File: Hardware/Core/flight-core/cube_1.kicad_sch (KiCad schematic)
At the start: 21 parts, among them J10 Conn_01x06, J11 Conn_01x04_Socket, J12 Conn_01x04_Socket, J13 Conn_01x06, J14 MicroFit_VT_3, J8 MicroFit_VT_3, J9 Cube Orange Plus Female Header, Q1 MMBF170, Q2 MMBF170, Q3 MMBF170

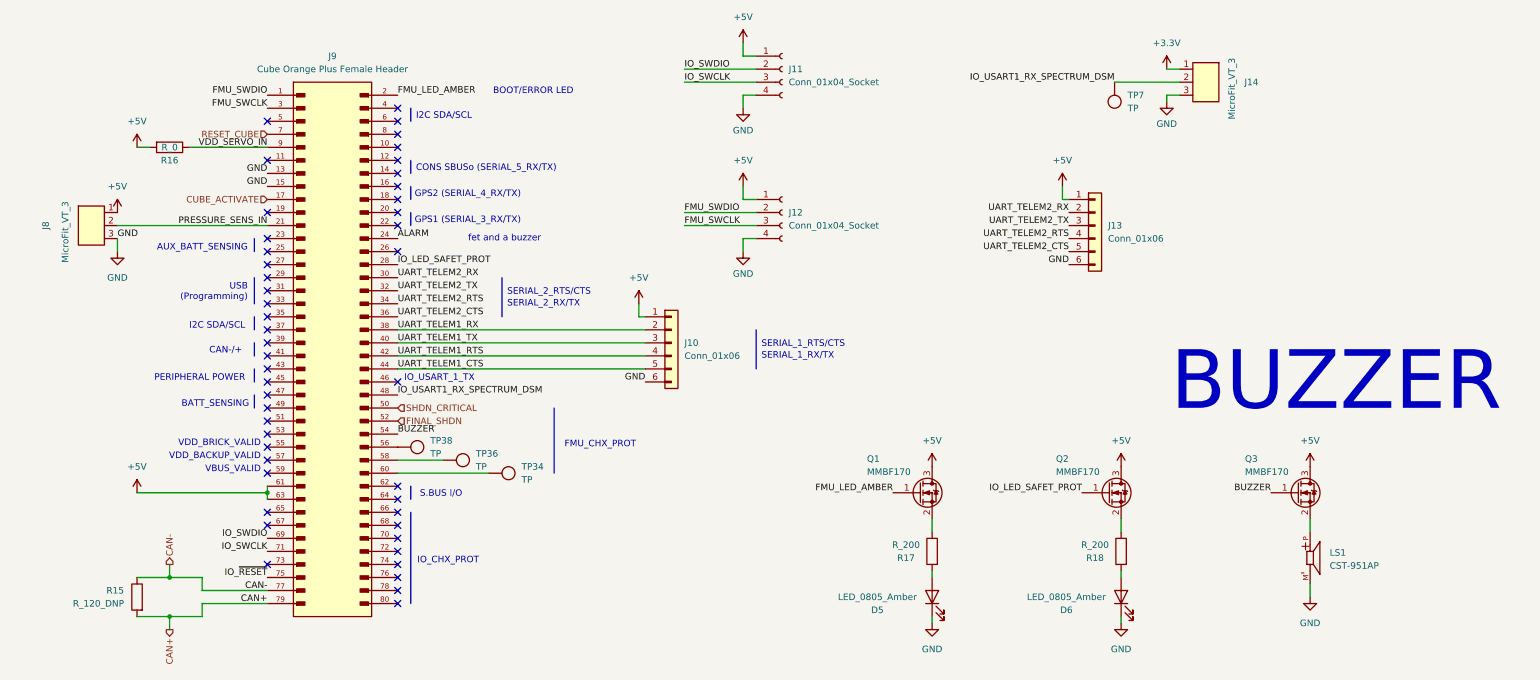
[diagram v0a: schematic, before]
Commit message: added sense pwr cycle pull down, low side cube mosfets, fixed mosi/miso swap on i/o expander, Rs -> generic, reannotated
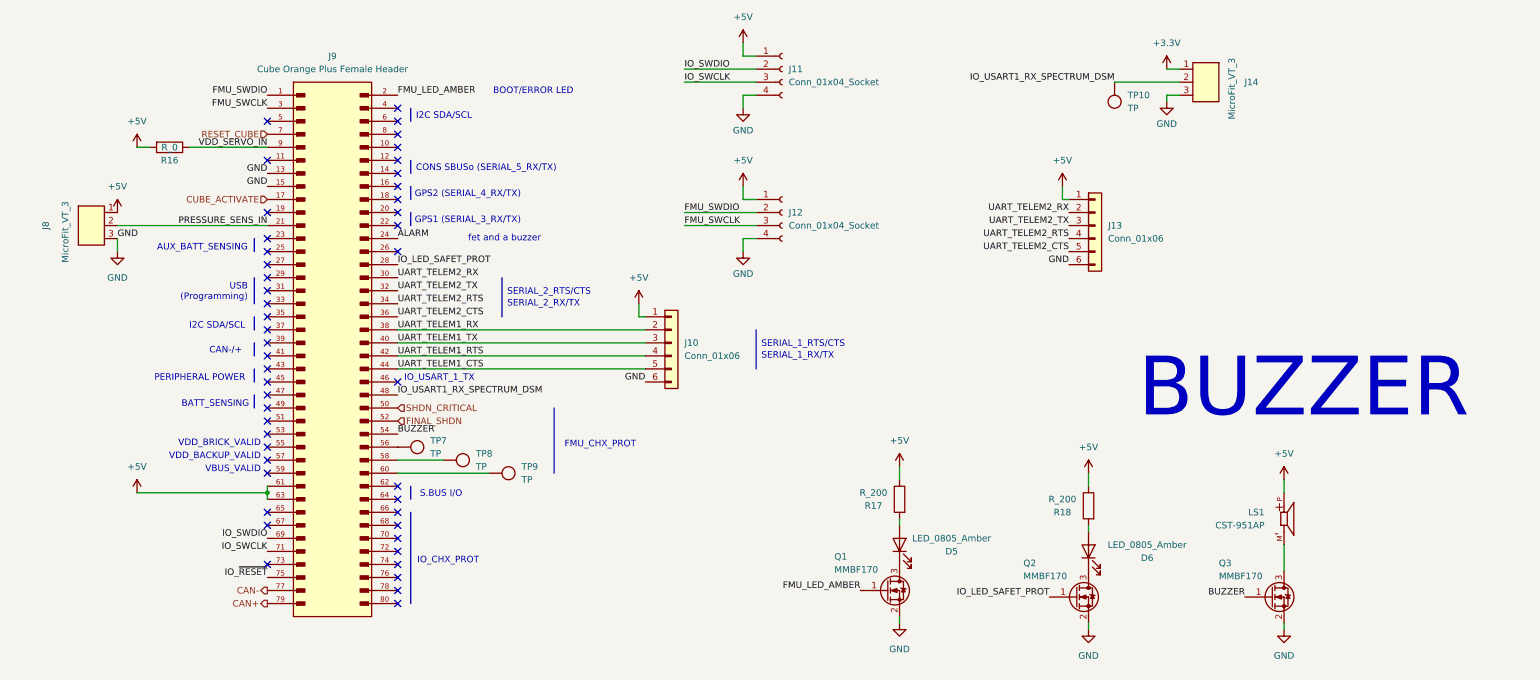
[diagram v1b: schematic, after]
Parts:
- removed R15: R_120_DNP, footprints:R_0603_1608Metric, symbol formula:R_120_DNP
- renumbered TP7 to TP10, TP38 to TP7, TP36 to TP8, TP34 to TP9
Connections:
- net +5V: now also LS1.P, R17.1, R18.1; no longer Q1.3 (D), Q2.3 (D), Q3.3 (D)
- net GND: now also Q1.2 (S), Q2.2 (S), Q3.2 (S); no longer D5.1 (K), D6.1 (K), LS1.M
- new net: LS1.M, Q3.3 (D)
- new net: D5.1 (K), Q1.3 (D)
- new net: D6.1 (K), Q2.3 (D)
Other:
- moved on the sheet: D5, D6, LS1, Q1, Q2, Q3, R17, R18

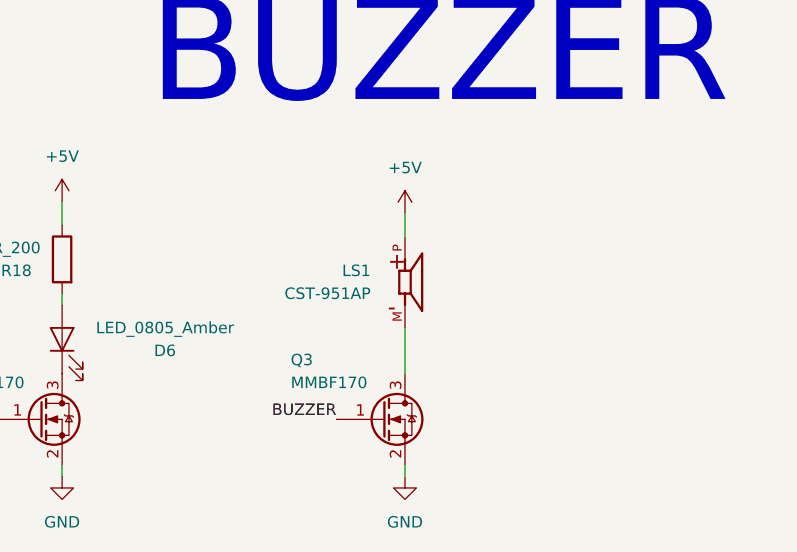
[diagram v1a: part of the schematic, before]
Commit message: replicated layout for all can repeaters, placed in shutdown order; added rider lower estop in schem; j18 is 4 pin
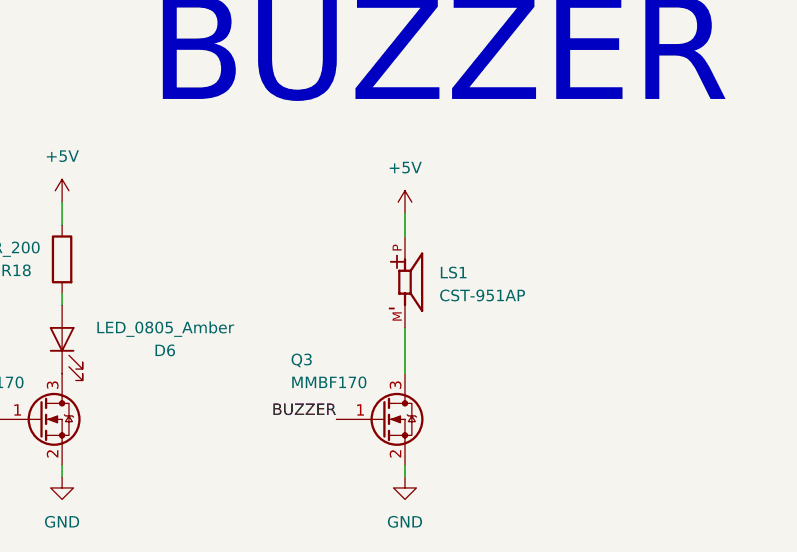
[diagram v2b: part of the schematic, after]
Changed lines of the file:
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@@
 		(dnp no)
 		(property "Reference" "LS1"
-			(at 265.43 132.08 0)
+			(at 273.05 132.327 0)
 			(effects
 				(font
 					(size 1.27 1.27)
 				)
-				(justify right)
+				(justify left)
 			)
 		)
 		(property "Value" "CST-951AP"
-			(at 265.43 134.62 0)
+			(at 273.05 134.867 0)
 			(effects
 				(font
 					(size 1.27 1.27)
 				)
-				(justify right)
+				(justify left)
 			)
 		)

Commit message: major component area placement begun, installing place footprints plugin, updating connectors to vertical
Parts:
- removed J10, J13: Conn_01x06, footprints:MicroFit_VT_6, symbol Connector_Generic:Conn_01x06
- added J10: Conn_02x06_Counter_Clockwise, Connector_Molex:Molex_Micro-Fit_3.0_43045-1212_2x06_P3.00mm_Vertical, symbol Connector_Generic:Conn_02x06_Counter_Clockwise
- renumbered J14 to J13
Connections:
- net +5V: now also J10.1 (Pin_1), J10.12 (Pin_12)
- net ALARM: now also Q3.1 (G)
- net GND: now also J10.6 (Pin_6), J10.7 (Pin_7)
- net UART_TELEM1_CTS: now also J10.5 (Pin_5)
- net UART_TELEM1_RTS: now also J10.4 (Pin_4)
- net UART_TELEM1_RX: now also J10.2 (Pin_2)
- net UART_TELEM1_TX: now also J10.3 (Pin_3)
- net UART_TELEM2_CTS: now also J10.8 (Pin_8)
- net UART_TELEM2_RTS: now also J10.9 (Pin_9)
- net UART_TELEM2_RX: now also J10.11 (Pin_11)
- net UART_TELEM2_TX: now also J10.10 (Pin_10)
- net BUZZER renamed CUBE_HANDOFF
- net CUBE_HANDOFF: no longer Q3.1 (G)
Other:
- note removed: "BUZZER"
- moved on the sheet: D5, D6, J11, J12, LS1, Q1, Q2, Q3, R17, R18

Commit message: switching test points to correct footprint and alternative symbol, moving leds
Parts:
- TP10, TP7, TP8, TP9: footprint footprints:tp_1.6mm -> TestPoint:TestPoint_Pad_D1.0mm; symbol formula:TP -> OlinBAD:D1.0_TP
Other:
- moved on the sheet: TP10, TP7, TP8, TP9
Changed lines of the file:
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@@
 	(wire
 		(pts
-			(xy 96.52 121.92) (xy 105.41 121.92)
+			(xy 96.52 121.92) (xy 111.76 121.92)
 		)
 		(stroke
@@
 	(wire
 		(pts
-			(xy 96.52 124.46) (xy 114.3 124.46)
+			(xy 96.52 124.46) (xy 116.84 124.46)
+		)
+		(stroke
+			(width 0)
+			(type default)
+		)
+	)
+	(wire
+		(pts
+			(xy 96.52 119.38) (xy 105.41 119.38)
 		)
 		(stroke
@@
 	)
 	(symbol
-		(lib_id "formula:TP")
-		(at 110.49 121.92 270)
+		(lib_id "OlinBAD:D1.0_TP")
+		(at 111.76 121.92 270)
 		(unit 1)
 		(exclude_from_sim no)
@@
 		(fields_autoplaced yes)
 		(property "Reference" "TP8"
-			(at 111.76 120.6499 90)
+			(at 116.84 120.6499 90)
 			(effects
 				(font
@@
 		)
 		(property "Value" "TP"
-			(at 111.76 123.1899 90)
+			(at 116.84 123.1899 90)
 			(effects
 				(font
@@
 			)
 		)
-		(property "Footprint" "footprints:tp_1.6mm"
-			(at 107.95 119.38 0)
-			(effects
-				(font
-					(size 1.27 1.27)
-				)
-				(hide yes)
-			)
-		)
-		(property "Datasheet" "http://www.keyelco.com/product-pdf.cfm?p=1314"
-			(at 110.49 121.92 0)
-			(effects
-				(font
-					(size 1.27 1.27)
-				)
-				(hide yes)
-			)
-		)
-		(property "Description" ""
-			(at 110.49 121.92 0)
+		(property "Footprint" "TestPoint:TestPoint_Pad_D1.0mm"
+			(at 111.76 127 0)
+			(effects
+				(font
+					(size 1.27 1.27)
+				)
+				(hide yes)
+			)
+		)
+		(property "Datasheet" "~"
+			(at 111.76 127 0)
+			(effects
+				(font
+					(size 1.27 1.27)
+				)
+				(hide yes)
+			)
+		)
+		(property "Description" "test point"
+			(at 111.76 121.92 0)
 			(effects
 				(font
@@
 		)
 		(property "MFN" "DK"
-			(at 113.03 124.46 0)
+			(at 114.3 124.46 0)
 			(effects
 				(font
@@
 		)
 		(property "MPN" "36-5006-ND"
-			(at 115.57 127 0)
+			(at 116.84 127 0)
 			(effects
 				(font
@@
 		)
 		(property "PurchasingLink" "https://www.digikey.com/product-detail/en/keystone-electronics/5006/36-5006-ND/255330"
-			(at 118.11 129.54 0)
+			(at 119.38 129.54 0)
 			(effects
 				(font
@@
 	)
 	(symbol
-		(lib_id "formula:TP")
-		(at 101.6 119.38 270)
+		(lib_id "OlinBAD:D1.0_TP")
+		(at 105.41 119.38 270)
 		(unit 1)
 		(exclude_from_sim no)
@@
 		(on_board yes)
 		(dnp no)
-		(fields_autoplaced yes)
 		(property "Reference" "TP7"
-			(at 102.87 118.1099 90)
+			(at 110.49 118.1099 90)
 			(effects
 				(font
@@
 		)
 		(property "Value" "TP"
-			(at 102.87 120.6499 90)
+			(at 110.49 120.6499 90)
 			(effects
 				(font
@@
 			)
 		)
-		(property "Footprint" "footprints:tp_1.6mm"
-			(at 99.06 116.84 0)
-			(effects
-				(font
-					(size 1.27 1.27)
-				)
-				(hide yes)
-			)
-		)
-		(property "Datasheet" "http://www.keyelco.com/product-pdf.cfm?p=1314"
-			(at 101.6 119.38 0)
-			(effects
-				(font
-					(size 1.27 1.27)
-				)
-				(hide yes)
-			)
-		)
-		(property "Description" ""
-			(at 101.6 119.38 0)
+		(property "Footprint" "TestPoint:TestPoint_Pad_D1.0mm"
+			(at 105.41 124.46 0)
+			(effects
+				(font
+					(size 1.27 1.27)
+				)
+				(hide yes)
+			)
+		)
+		(property "Datasheet" "~"
+			(at 105.41 124.46 0)
+			(effects
+				(font
+					(size 1.27 1.27)
+				)
+				(hide yes)
+			)
+		)
+		(property "Description" "test point"
+			(at 105.41 119.38 0)
 			(effects
 				(font
@@
 		)
 		(property "MFN" "DK"
-			(at 104.14 121.92 0)
+			(at 107.95 121.92 0)
 			(effects
 				(font
@@
 		)
 		(property "MPN" "36-5006-ND"
-			(at 106.68 124.46 0)
+			(at 110.49 124.46 0)
 			(effects
 				(font
@@
 		)
 		(property "PurchasingLink" "https://www.digikey.com/product-detail/en/keystone-electronics/5006/36-5006-ND/255330"
-			(at 109.22 127 0)
+			(at 113.03 127 0)
 			(effects
 				(font
@@
 	)
 	(symbol
-		(lib_id "formula:TP")
-		(at 236.22 53.34 180)
+		(lib_id "OlinBAD:D1.0_TP")
+		(at 236.22 48.26 180)
 		(unit 1)
 		(exclude_from_sim no)
@@
 		(fields_autoplaced yes)
 		(property "Reference" "TP10"
-			(at 238.76 50.7999 0)
+			(at 238.76 50.2919 0)
 			(effects
 				(font
@@
 		)
 		(property "Value" "TP"
-			(at 238.76 53.3399 0)
+			(at 238.76 52.8319 0)
 			(effects
 				(font
@@
 			)
 		)
-		(property "Footprint" "footprints:tp_1.6mm"
-			(at 238.76 50.8 0)
-			(effects
-				(font
-					(size 1.27 1.27)
-				)
-				(hide yes)
-			)
-		)
-		(property "Datasheet" "http://www.keyelco.com/product-pdf.cfm?p=1314"
-			(at 236.22 53.34 0)
-			(effects
-				(font
-					(size 1.27 1.27)
-				)
-				(hide yes)
-			)
-		)
-		(property "Description" ""
-			(at 236.22 53.34 0)
+		(property "Footprint" "TestPoint:TestPoint_Pad_D1.0mm"
+			(at 231.14 48.26 0)
+			(effects
+				(font
+					(size 1.27 1.27)
+				)
+				(hide yes)
+			)
+		)
+		(property "Datasheet" "~"
+			(at 231.14 48.26 0)
+			(effects
+				(font
+					(size 1.27 1.27)
+				)
+				(hide yes)
+			)
+		)
+		(property "Description" "test point"
+			(at 236.22 48.26 0)
 			(effects
 				(font
@@
 		)
 		(property "MFN" "DK"
-			(at 233.68 55.88 0)
+			(at 233.68 50.8 0)
 			(effects
 				(font
@@
 		)
 		(property "MPN" "36-5006-ND"
-			(at 231.14 58.42 0)
+			(at 231.14 53.34 0)
 			(effects
 				(font
@@
 		)
 		(property "PurchasingLink" "https://www.digikey.com/product-detail/en/keystone-electronics/5006/36-5006-ND/255330"
-			(at 228.6 60.96 0)
+			(at 228.6 55.88 0)
 			(effects
 				(font
@@
 	)
 	(symbol
-		(lib_id "formula:TP")
-		(at 119.38 124.46 270)
+		(lib_id "OlinBAD:D1.0_TP")
+		(at 116.84 124.46 270)
 		(unit 1)
 		(exclude_from_sim no)
@@
 		(fields_autoplaced yes)
 		(property "Reference" "TP9"
-			(at 120.65 123.1899 90)
+			(at 121.92 123.1899 90)
 			(effects
 				(font
@@
 		)
 		(property "Value" "TP"
-			(at 120.65 125.7299 90)
+			(at 121.92 125.7299 90)
 			(effects
 				(font
@@
 			)
 		)
-		(property "Footprint" "footprints:tp_1.6mm"
-			(at 116.84 121.92 0)
-			(effects
-				(font
-					(size 1.27 1.27)
-				)
-				(hide yes)
-			)
-		)
-		(property "Datasheet" "http://www.keyelco.com/product-pdf.cfm?p=1314"
-			(at 119.38 124.46 0)
-			(effects
-				(font
-					(size 1.27 1.27)
-				)
-				(hide yes)
-			)
-		)
-		(property "Description" ""
-			(at 119.38 124.46 0)
+		(property "Footprint" "TestPoint:TestPoint_Pad_D1.0mm"
+			(at 116.84 129.54 0)
+			(effects
+				(font
+					(size 1.27 1.27)
+				)
+				(hide yes)
+			)
+		)
+		(property "Datasheet" "~"
+			(at 116.84 129.54 0)
+			(effects
+				(font
+					(size 1.27 1.27)
+				)
+				(hide yes)
+			)
+		)
+		(property "Description" "test point"
+			(at 116.84 124.46 0)
 			(effects
 				(font
@@
 		)
 		(property "MFN" "DK"
-			(at 121.92 127 0)
+			(at 119.38 127 0)
 			(effects
 				(font
@@
 		)
 		(property "MPN" "36-5006-ND"
-			(at 124.46 129.54 0)
+			(at 121.92 129.54 0)
 			(effects
 				(font
@@
 		)
 		(property "PurchasingLink" "https://www.digikey.com/product-detail/en/keystone-electronics/5006/36-5006-ND/255330"
-			(at 127 132.08 0)
-			(effects
-				(font
+			(at 124.46 132.08 0)
+			(effects
+				(font

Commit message: updating mini tps to new symbol and footprint
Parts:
- TP10, TP7, TP8, TP9: footprint TestPoint:TestPoint_Pad_D1.0mm -> obad_footprints:TestPoint_Pad_D1.0mm
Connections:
- net +5V: now also D5.2 (A), D6.2 (A); no longer R17.1, R18.1
- net GND: now also R17.2, R18.2; no longer Q1.2 (S), Q2.2 (S)
- new net: Q2.2 (S), R18.1
- new net: Q1.2 (S), R17.1
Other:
- moved on the sheet: D5, D6, Q1, Q2, R17, R18

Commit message: Major reroute & semi-final update
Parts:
- removed J12: Conn_01x04_Socket, Connector_PinSocket_2.54mm:PinSocket_1x04_P2.54mm_Vertical, symbol Connector:Conn_01x04_Socket
- removed J13, J8: MicroFit_VT_3, footprints:MicroFit_VT_3, symbol formula:MicroFit_VT_3
- removed TP10: TP, obad_footprints:TestPoint_Pad_D1.0mm, symbol OlinBAD:D1.0_TP
- added J501: Conn_02x02_Counter_Clockwise, Connector_Molex:Molex_Micro-Fit_3.0_43045-0412_2x02_P3.00mm_Vertical, symbol Connector_Generic:Conn_02x02_Counter_Clockwise
- added J502: Conn_01x04_Socket, Connector_PinSocket_2.54mm:PinSocket_1x04_P2.54mm_Vertical, symbol Connector:Conn_01x04_Socket
- added J503: Conn_01x03, Connector_Molex:Molex_Micro-Fit_3.0_43650-0315_1x03_P3.00mm_Vertical, symbol Connector_Generic:Conn_01x03
- renumbered Q1 to Q501, Q2 to Q502, R17 to R501, R18 to R502
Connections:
- net +5V: now also J501.1 (Pin_1), J502.1 (Pin_1), J503.3 (Pin_3)
- net FMU_SWCLK: now also J502.3 (Pin_3)
- net FMU_SWDIO: now also J502.2 (Pin_2)
- net GND: now also Q501.2 (S), Q502.2 (S), J501.2 (Pin_2), J502.4 (Pin_4), J503.1 (Pin_1); no longer R501.2, R502.2
- net IO_USART1_RX_SPECTRUM_DSM: no longer J9.48
- net PRESSURE_SENS_IN: now also J503.2 (Pin_2)
- net at D5.1 (K): now also R501.1; no longer Q501.3 (D)
- net at R502.1: now also D6.1 (K); no longer Q502.2 (S)
- net at Q502.3 (D): now also R502.2; no longer D6.1 (K)
- net SBUS_IO_A: now reaches J9.62
- net SBUS_IO_A: now also J501.4 (Pin_4)
- net SBUS_IO_B: now reaches J9.64
- net SBUS_IO_B: now also J501.3 (Pin_3)
- new net: Q501.3 (D), R501.2
- no-connect marks 47 -> 46
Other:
- note added: "IO_USART1_RX_SPECTRUM_DSM"
- moved on the sheet: Q501, Q502, R501, R502

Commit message: minor reformatting; no substantial changes
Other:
- note removed: "SERIAL_1_RTS/CTS"
- note removed: "SERIAL_1_RX/TX"
- moved on the sheet: D5, D6, J10, J11, J501, J502, J503, J9, LS1, Q3, Q501, Q502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
